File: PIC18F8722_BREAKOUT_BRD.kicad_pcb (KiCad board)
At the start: 2 copper layers, 92.1 x 66 mm, 33 parts, among them IC1 PIC18F8722, P1 PGM_CONN, P12 PWR_CON, P2 CONN_16, P3 CONN_5, P4 CONN_16, P5 CONN_16, P6 CONN_16, P7 PWR_CON, P9 PWR_CON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

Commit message: Updated as per requirement
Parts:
- removed the 1PIN at (193.0, 100.3)
- removed the 1PIN at (130.8, 100.3)
- removed the 1PIN at (130.8, 151.1)
- removed the 1PIN at (193.0, 151.1)
- removed P12: PWR_CON, mors_2p
- removed P6: CONN_16, SIL-16
- D1: value HB_LED -> LED
- P2: value CONN_16 -> CONN _1_20; footprint SIL-16 -> SIL-20
- P3: value CONN_5 -> CONN_21_40; footprint SIL-5 -> SIL-20
- P4: value CONN_16 -> CONN_41_60; footprint SIL-16 -> SIL-20
- P5: value CONN_16 -> CONN_61_80; footprint SIL-16 -> SIL-20
- P7: footprint SIL-2 -> mors_2p
- R1: moved to B.Cu
- moved P7 97.0 mm to (114.9, 86.6), turned to 270 degrees
- moved P2 67.9 mm to (123.7, 119.6), turned to 270 degrees
- moved C6 62.8 mm to (126.5, 80.2)
- moved C7 62.8 mm to (123.0, 80.2)
- moved P3 61.8 mm to (165.2, 153.4)
- moved P4 57.9 mm to (192.0, 104.6), turned to 90 degrees
- moved P5 56.8 mm to (149.9, 72.2), turned to 180 degrees
- moved R4 56.1 mm to (196.7, 123.2), turned to 270 degrees
- moved C8 54.6 mm to (196.8, 129.4), turned to 90 degrees
- moved R1 34.7 mm to (164.0, 147.8), turned to 180 degrees
- moved SW1 31.9 mm to (116.0, 98.7), turned to 0 degrees
- moved 1PIN 23.8 mm to (195.6, 71.6)
- moved 1PIN 23.3 mm to (114.9, 71.9)
- moved C2 13.2 mm to (160.5, 115.8)
- moved C3 13.2 mm to (161.2, 111.7)
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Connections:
- C1 pad 1: /VCC -> /AVDD
- C2 pad 1: /VCC -> /AVDD
- C3 pad 1: /VCC -> /AVDD
- C4 pad 1: /VCC -> /AVDD
- C5 pad 1: /VCC -> /AVDD
- C6 pad 1: /VCC -> /AVDD
- C7 pad 1: /VCC -> /AVDD
- IC1 pad 12: /VCC -> /AVDD
- IC1 pad 25: /VCC -> /AVDD
- IC1 pad 32: /VCC -> /AVDD
- IC1 pad 48: /VCC -> /AVDD
- IC1 pad 71: /VCC -> /AVDD
- P1 pad 2: /VCC -> /AVDD
- P2 pad 1: /RA0 -> /RH2
- P2 pad 10: /RB1 -> /RG4
- P2 pad 11: /RB2 -> GND
- P2 pad 12: /RB3 -> /AVDD
- P2 pad 13: /RB4 -> /RF7
- P2 pad 14: /RB5 -> /RF6
- P2 pad 15: /PGC -> /RF5
- P2 pad 16: /PGD -> /RF4
- P2 pad 2: /RA1 -> /RH3
- P2 pad 3: /RA2 -> /RE1
- P2 pad 4: /RA3 -> /RE0
- P2 pad 5: /RA4 -> /HB_LED
- P2 pad 6: /RA5 -> /RG1
- P2 pad 7: /RA6 -> /RG2
- P2 pad 8: /RA7 -> /RG3
- P2 pad 9: /RB0 -> /MCLR
- P3 pad 1: /HB_LED -> /RH5
- P3 pad 2: /RG1 -> /RH4
- P3 pad 3: /RG2 -> /RF1
- P3 pad 4: /RG3 -> /RF0
- P3 pad 5: /RG4 -> /AVDD
- P4 pad 1: /RC0 -> /RJ6
- P4 pad 10: /RD1 -> /RA6
- P4 pad 11: /RD2 -> GND
- P4 pad 12: /RD3 -> /PGC
- P4 pad 13: /RD4 -> /RB5
- P4 pad 14: /RD5 -> /RB4
- P4 pad 15: /RD6 -> /RB3
- P4 pad 16: /RD7 -> /RB2
- P4 pad 2: /RC1 -> /RJ7
- P4 pad 7: /RC6 -> /PGD
- P4 pad 8: /RC7 -> /AVDD
- P4 pad 9: /RD0 -> /RA7
- P5 pad 1: /RE0 -> /RJ1
- P5 pad 10: /RF1 -> GND
- P5 pad 11: /RF2 -> /AVDD
- P5 pad 12: /RF3 -> /RD0
- P5 pad 13: /RF4 -> /RE7
- P5 pad 14: /RF5 -> /RE6
- P5 pad 15: /RF6 -> /RE5
- P5 pad 16: /RF7 -> /RE4
- P5 pad 2: /RE1 -> /RJ0
- P5 pad 3: /RE2 -> /RD7
- P5 pad 4: /RE3 -> /RD6
- P5 pad 5: /RE4 -> /RD5
- P5 pad 6: /RE5 -> /RD4
- P5 pad 7: /RE6 -> /RD3
- P5 pad 8: /RE7 -> /RD2
- P5 pad 9: /RF0 -> /RD1
- P7 pad 2: /VCC -> /AVDD
- P9 pad 2: /VCC -> /AVDD
- R1 pad 1: /VCC -> /AVDD
- R2 pad 1: /VCC -> /AVDD
- R3 pad 1: /VCC -> /AVDD
- R4 pad 1: /VCC -> /AVDD
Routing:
- net /VCC: track 295.1 -> 0.00 mm, vias 5 -> 0
- net /AVDD: track 0.00 -> 207.5 mm, vias 0 -> 5
- net GND: track 41.1 -> 189.5 mm, vias 8 -> 4
- net /RD0: track 83.2 -> 34.8 mm, vias 2 -> 0
- net /RD1: track 81.6 -> 34.7 mm, vias 2 -> 0
- net /RD2: track 81.1 -> 35.5 mm, vias 2 -> 0
- net /RD3: track 80.6 -> 36.4 mm, vias 2 -> 0
- net /RD4: track 79.9 -> 37.2 mm, vias 2 -> 0
- net /RD5: track 79.3 -> 38.1 mm, vias 2 -> 0
- net /RD6: track 78.8 -> 38.9 mm, vias 2 -> 0
- net /RD7: track 76.1 -> 39.7 mm, vias 2 -> 0
- net /MCLR: track 201.1 -> 165.2 mm, vias 3 -> 0
- net /RJ4: track 70.3 -> 41.6 mm, vias 2 -> 0
- net /RJ5: track 65.8 -> 42.5 mm, vias 3 -> 0
- net /RJ6: track 57.1 -> 35.7 mm, vias 3 -> 0
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- added copper zone on F.Cu, net /AVDD
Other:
- board outline removed
- board text removed: "RA0"
- board text removed: "RB0"
- board text removed: "RC0"
- board text removed: "RD0"
- board text removed: "RE0"
- board text removed: "RF0"
- board text removed: "RG0"
- board text removed: "RH0"
- board text removed: "RJ0"

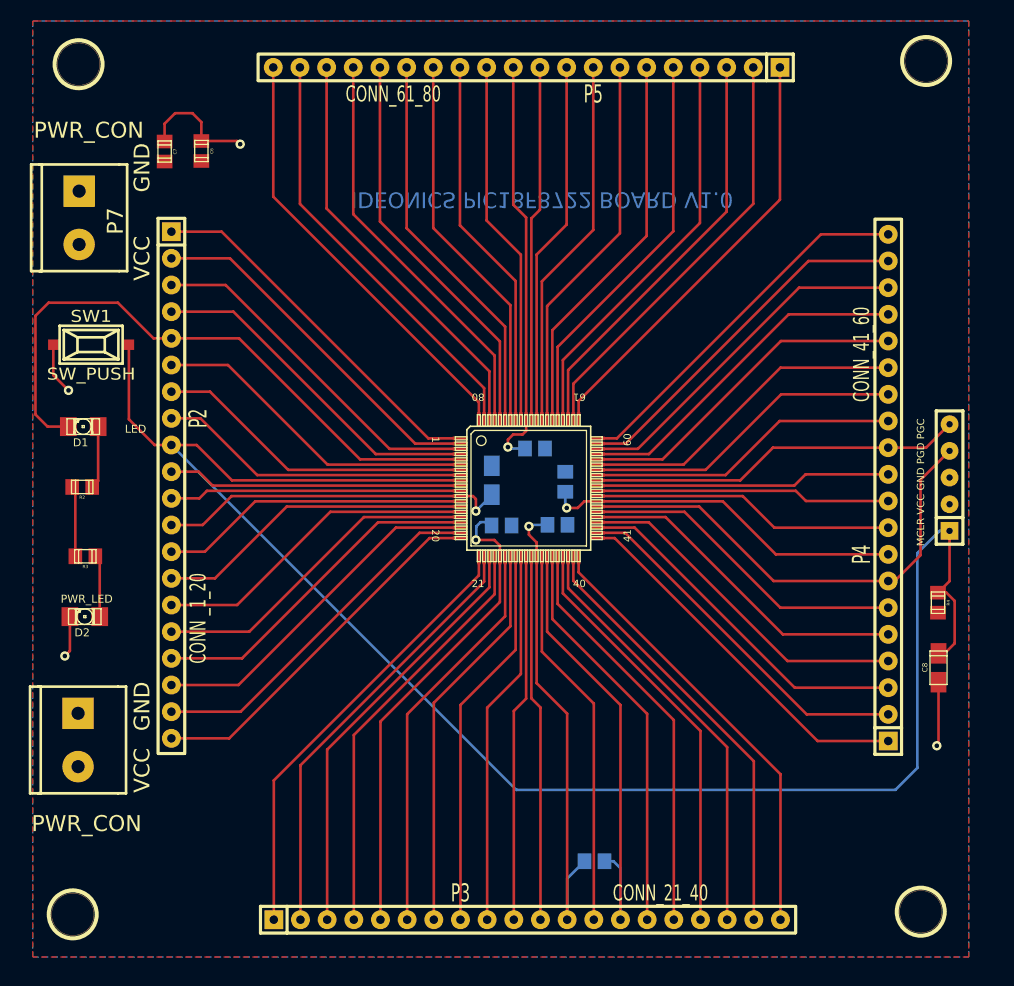
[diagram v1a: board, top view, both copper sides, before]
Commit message: Via dimension updated
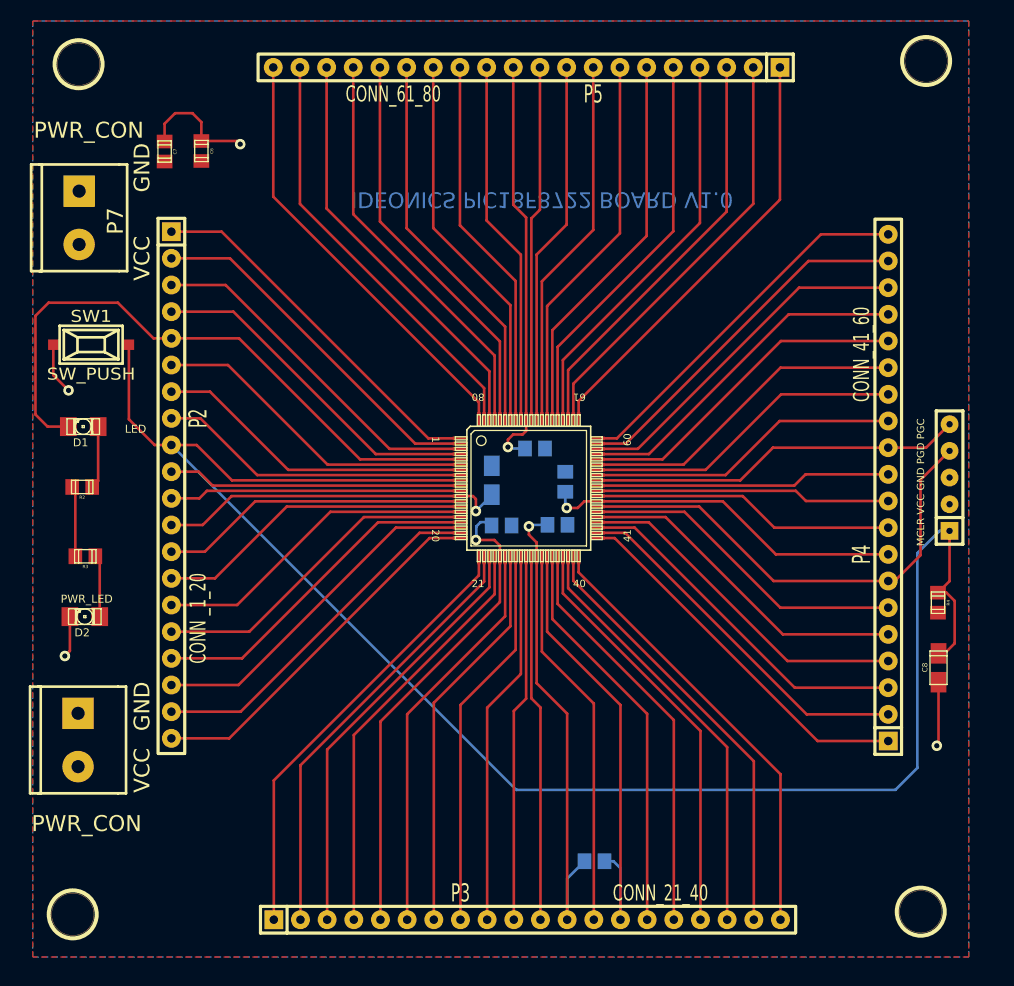
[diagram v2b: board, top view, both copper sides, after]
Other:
- net class Default: via_dia 0.889 -> 1
- net class VCC: via_dia 0.889 -> 1
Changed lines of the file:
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@@
     (links 125)
     (no_connects 0)
-    (area 0 0 0 0)
+    (area 109.371734 67.311599 213 167.7)
     (thickness 1.6)
     (drawings 20)
@@
     (segment_width 0.2)
     (edge_width 0.1)
-    (via_size 0.889)
+    (via_size 1)
     (via_drill 0.635)
     (via_min_size 0.1)
@@
     (clearance 0.17)
     (trace_width 0.254)
-    (via_dia 0.889)
+    (via_dia 1)
     (via_drill 0.635)
     (uvia_dia 0.508)
@@
     (clearance 0.17)
     (trace_width 1)
-    (via_dia 0.889)
+    (via_dia 1)
     (via_drill 0.635)
     (uvia_dia 0.508)
@@
   (segment (start 161.2124 114.0624) (end 161.2124 112.6505) (width 0.254) (layer B.Cu) (net 1))
   (segment (start 161.35 114.2) (end 161.2124 114.0624) (width 0.254) (layer B.Cu) (net 1))
-  (via (at 161.35 114.2) (size 0.889) (layers F.Cu B.Cu) (net 1))
+  (via (at 161.35 114.2) (size 1) (layers F.Cu B.Cu) (net 1))
   (segment (start 162.4 114.2) (end 161.35 114.2) (width 0.254) (layer F.Cu) (net 1))
   (segment (start 163.03152 113.56848) (end 162.4 114.2) (width 0.254) (layer F.Cu) (net 1))
@@
   (segment (start 158.4833 117.4833) (end 157.75 116.75) (width 0.254) (layer F.Cu) (net 1))
   (segment (start 157.75 116.75) (end 157.75 115.95) (width 0.254) (layer F.Cu) (net 1))
-  (via (at 157.75 115.95) (size 0.889) (layers F.Cu B.Cu) (net 1))
+  (via (at 157.75 115.95) (size 1) (layers F.Cu B.Cu) (net 1))
   (segment (start 157.75 115.95) (end 157.892 115.808) (width 0.254) (layer B.Cu) (net 1))
   (segment (start 157.892 115.808) (end 159.5199 115.808) (width 0.254) (layer B.Cu) (net 1))
@@
   (segment (start 152.75 117.2) (end 152.75 115.95) (width 0.254) (layer B.Cu) (net 1))
   (segment (start 152.7 117.25) (end 152.75 117.2) (width 0.254) (layer B.Cu) (net 1))
-  (via (at 152.7 117.25) (size 0.889) (layers F.Cu B.Cu) (net 1))
+  (via (at 152.7 117.25) (size 1) (layers F.Cu B.Cu) (net 1))
   (segment (start 154.45 117.25) (end 152.7 117.25) (width 0.254) (layer F.Cu) (net 1))
   (segment (start 154.98572 117.78572) (end 154.45 117.25) (width 0.254) (layer F.Cu) (net 1))
@@
   (segment (start 154.2124 112.9876) (end 154.2124 112.93214) (width 0.254) (layer B.Cu) (net 1))
   (segment (start 152.7 114.5) (end 154.2124 112.9876) (width 0.254) (layer B.Cu) (net 1))
-  (via (at 152.7 114.5) (size 0.889) (layers F.Cu B.Cu) (net 1))
+  (via (at 152.7 114.5) (size 1) (layers F.Cu B.Cu) (net 1))
   (segment (start 152.7 113.35) (end 152.7 114.5) (width 0.254) (layer F.Cu) (net 1))
   (segment (start 152.4181 113.0681) (end 152.7 113.35) (width 0.254) (layer F.Cu) (net 1))
@@
   (segment (start 155.888 108.538) (end 157.3799 108.538) (width 0.254) (layer B.Cu) (net 1))
   (segment (start 155.75 108.4) (end 155.888 108.538) (width 0.254) (layer B.Cu) (net 1))
-  (via (at 155.75 108.4) (size 0.889) (layers F.Cu B.Cu) (net 1))
+  (via (at 155.75 108.4) (size 1) (layers F.Cu B.Cu) (net 1))
   (segment (start 155.75 107.7) (end 155.75 108.4) (width 0.254) (layer F.Cu) (net 1))
   (segment (start 156.25 107.2) (end 155.75 107.7) (width 0.254) (layer F.Cu) (net 1))
@@
   (segment (start 196.7636 130.79494) (end 196.7636 136.6864) (width 0.254) (layer F.Cu) (net 72))
   (segment (start 196.6 136.85) (end 196.6 136.8) (width 0.254) (layer B.Cu) (net 72))
-  (via (at 196.6 136.85) (size 0.889) (layers F.Cu B.Cu) (net 72))
+  (via (at 196.6 136.85) (size 1) (layers F.Cu B.Cu) (net 72))
   (segment (start 196.7636 136.6864) (end 196.6 136.85) (width 0.254) (layer F.Cu) (net 72))
   (segment (start 112.45082 98.65) (end 112.45082 101.55082) (width 0.254) (layer F.Cu) (net 72))
-  (via (at 113.9 103) (size 0.889) (layers F.Cu B.Cu) (net 72))
+  (via (at 113.9 103) (size 1) (layers F.Cu B.Cu) (net 72))
   (segment (start 112.45082 101.55082) (end 113.9 103) (width 0.254) (layer F.Cu) (net 72))
   (segment (start 164.32784 112.06988) (end 183.03012 112.06988) (width 0.254) (layer F.Cu) (net 72))
@@
   (segment (start 158.8516 133.2016) (end 157.98292 132.33292) (width 0.254) (layer F.Cu) (net 72))
   (segment (start 114.03014 124.55) (end 114.03014 127.81986) (width 0.254) (layer F.Cu) (net 72))
-  (via (at 113.55 128.3) (size 0.889) (layers F.Cu B.Cu) (net 72))
+  (via (at 113.55 128.3) (size 1) (layers F.Cu B.Cu) (net 72))
   (segment (start 114.03014 127.81986) (end 113.55 128.3) (width 0.254) (layer F.Cu) (net 72))
   (segment (start 126.55 79.2475) (end 129.9475 79.2475) (width 0.254) (layer F.Cu) (net 72))
-  (via (at 130.25 79.55) (size 0.889) (layers F.Cu B.Cu) (net 72))
+  (via (at 130.25 79.55) (size 1) (layers F.Cu B.Cu) (net 72))
   (segment (start 129.9475 79.2475) (end 130.25 79.55) (width 0.254) (layer F.Cu) (net 72))
   (segment (start 123.05 79.2975) (end 123.05 77.6) (width 0.254) (layer F.Cu) (net 72))
